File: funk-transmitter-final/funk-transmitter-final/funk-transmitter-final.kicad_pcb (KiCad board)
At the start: 2 copper layers, 43.2 x 41.7 mm, 6 parts, among them J1 Conn_01x02_Socket, J2 Conn_01x02_Socket, J2 Conn_01x08_Socket, U1 Si4463_eigen

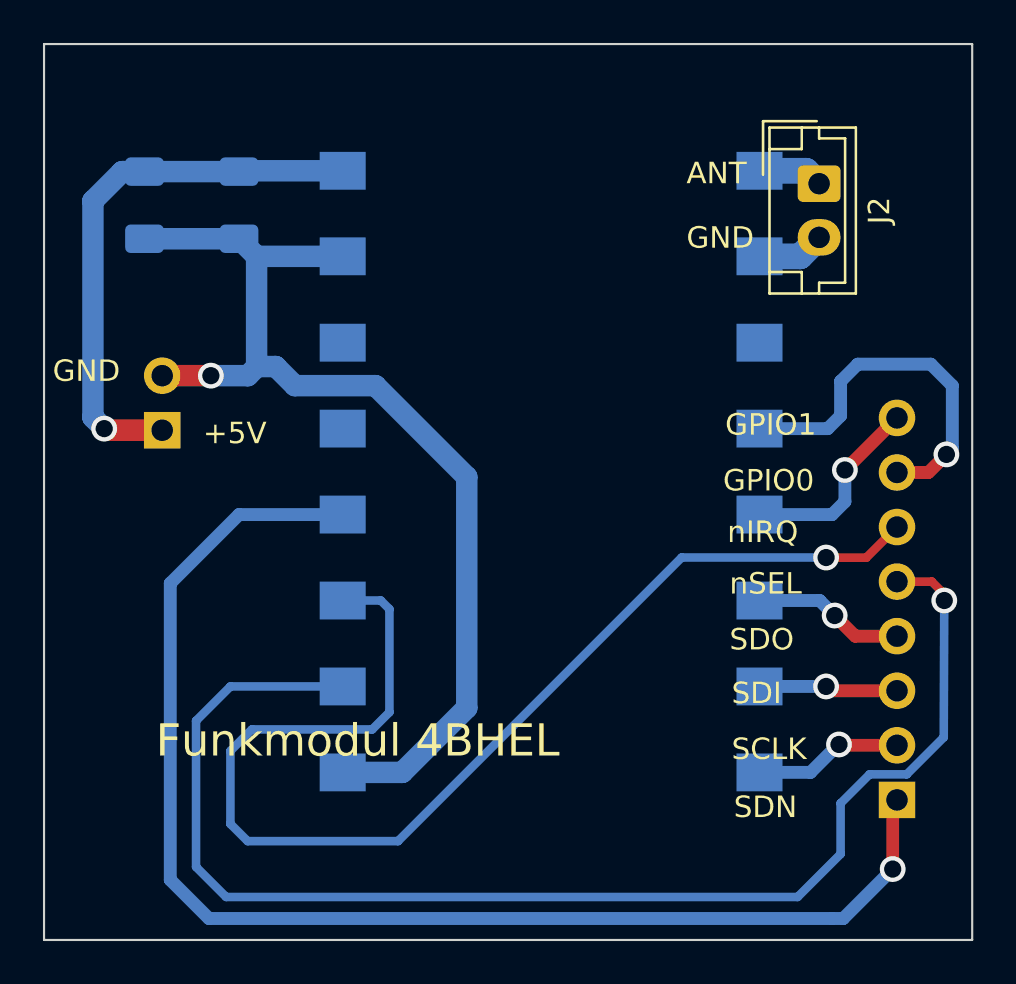
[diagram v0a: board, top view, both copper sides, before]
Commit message: display brain platine erweitert
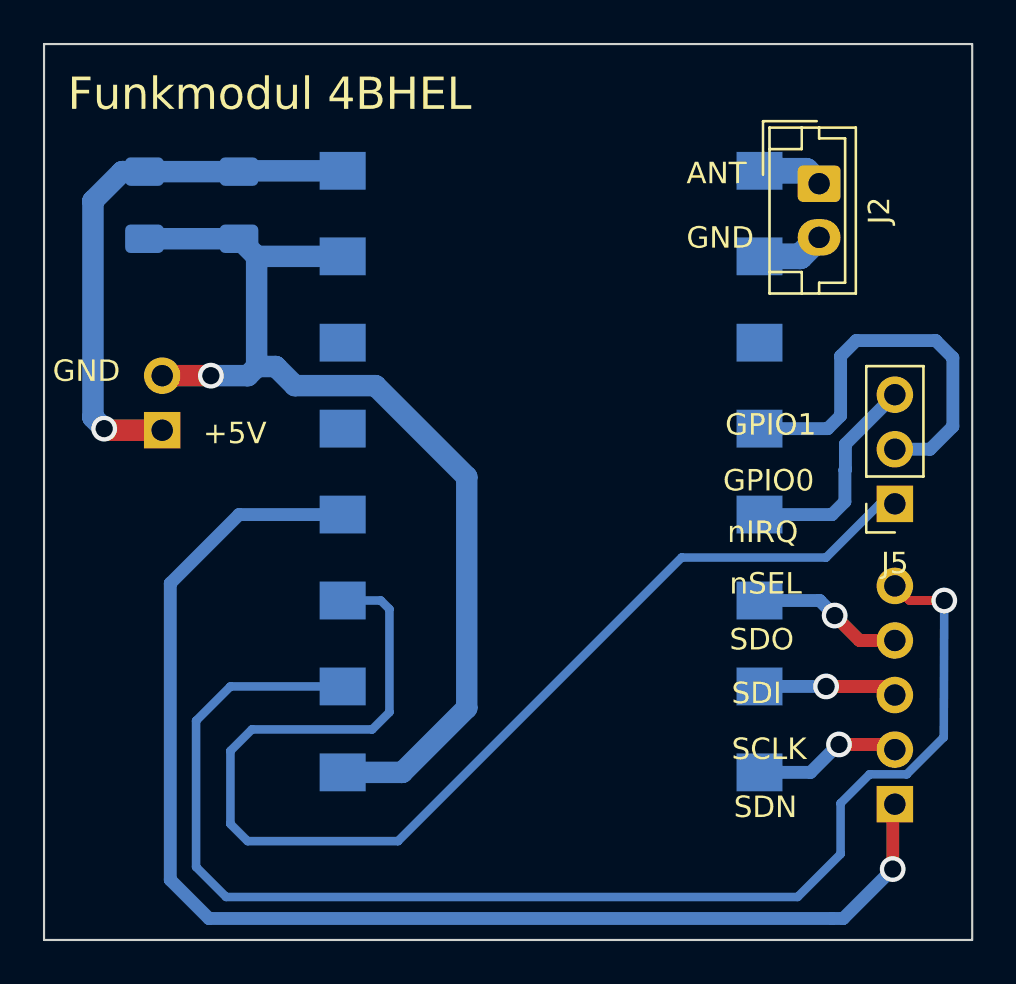
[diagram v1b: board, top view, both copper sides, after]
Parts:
- removed the J2 at (165.1, 115.7)
- added J4: Conn_01x05_Socket, Connector_PinHeader_2.54mm:PinHeader_1x05_P2.54mm_Vertical, B.Cu at (165.0, 115.9)
- added J5: Conn_01x03_Socket, Connector_PinSocket_2.54mm:PinSocket_1x03_P2.54mm_Vertical, F.Cu at (165.0, 101.9)
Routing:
- net /GPIO0: track 17.6 -> 18.8 mm, vias 1 -> 0
- net /GPIO1: track 8.99 -> 9.99 mm, vias 1 -> 0
- net /nIRQ: track 55.9 -> 56.3 mm, vias 1 -> 0
